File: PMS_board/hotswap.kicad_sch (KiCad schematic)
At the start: 22 parts, among them Q5 Q_NMOS_GDS, Q6 Q_NMOS_GDS, Q7 Q_NMOS_GDS, Q8 Q_NMOS_GDS, U12 LM74800QDRRRQ1, U9 LM74800QDRRRQ1

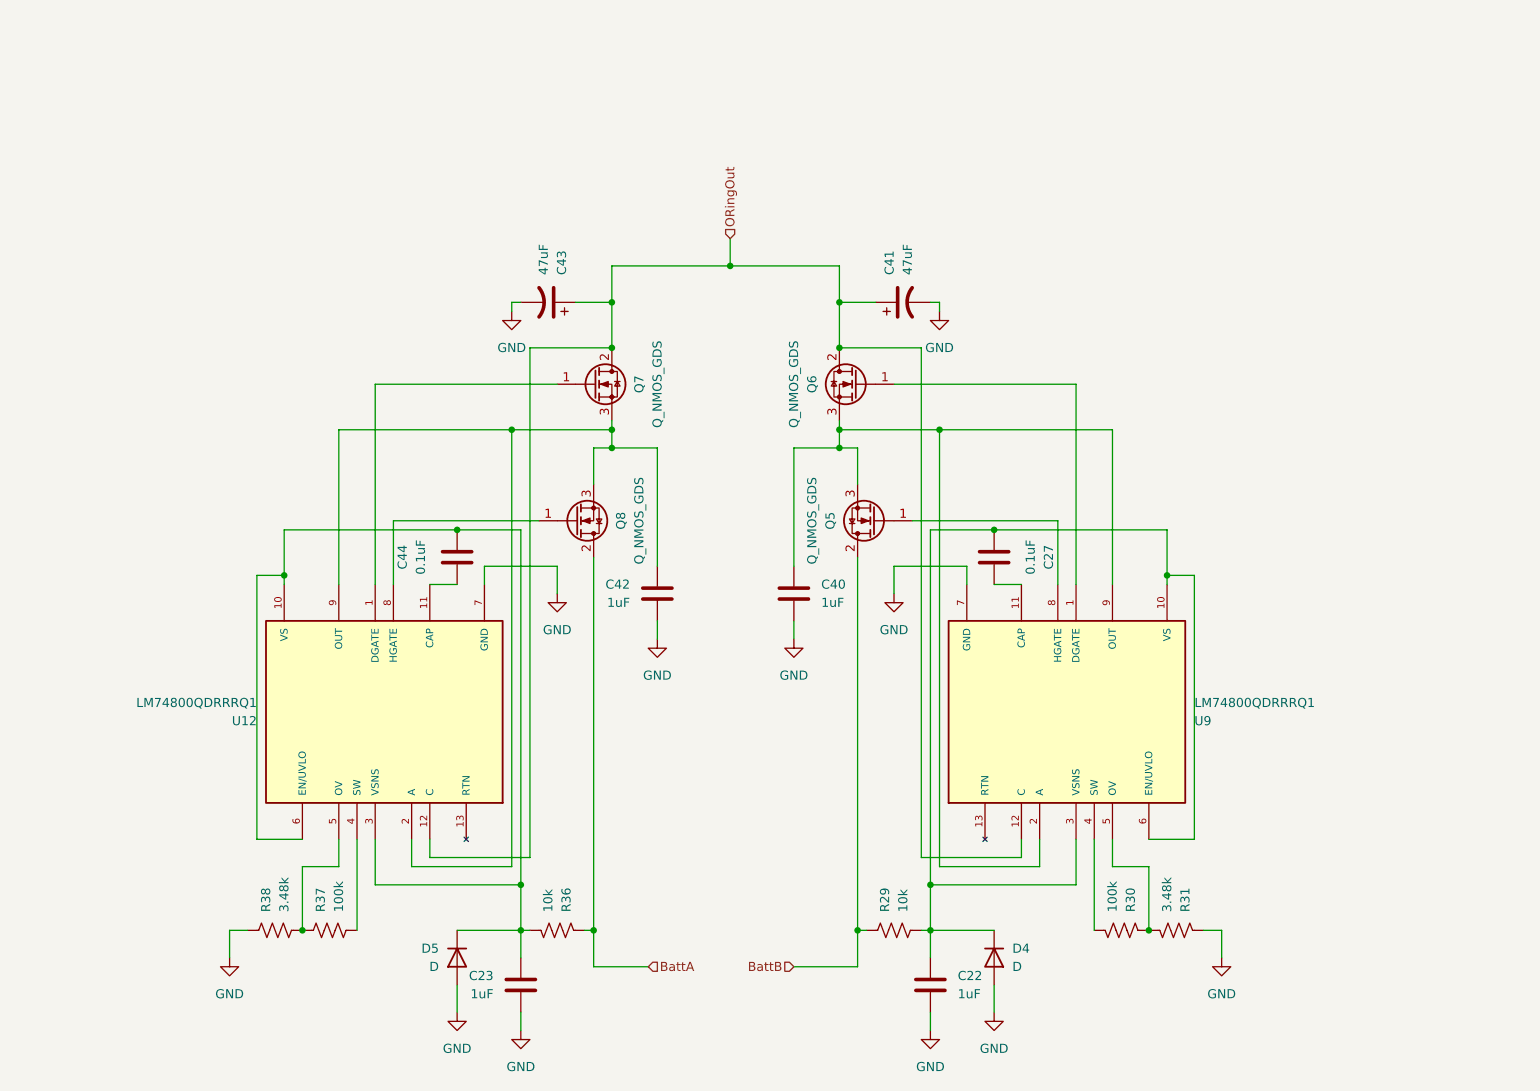
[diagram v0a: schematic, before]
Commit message: add power smoothing
I added the majority (i hope) of the necessary components for power smoothing and conversion. I also added notes to remind me and to inform others in my absence as to what still needs to be done to my knowledge.
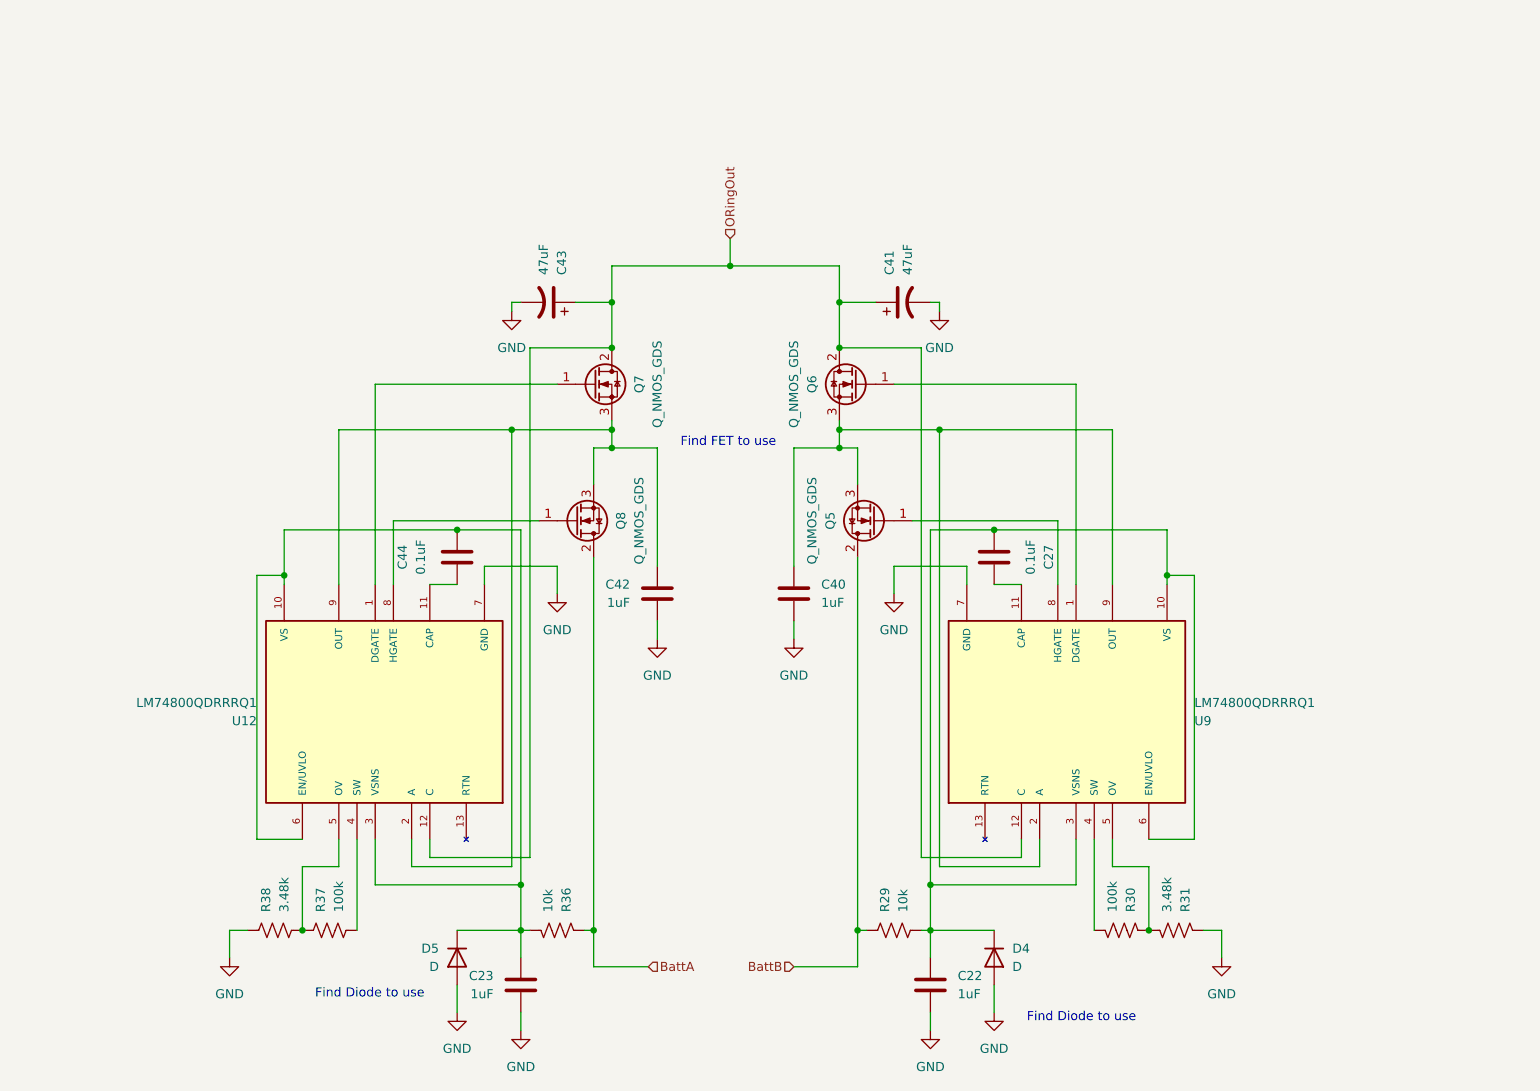
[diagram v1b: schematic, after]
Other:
- note added: "Find Diode to use"
- note added: "Find FET to use"
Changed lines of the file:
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@@
 	(generator_version "10.0")
 	(paper "A4")
+	(text "Find Diode to use\n"
+		(exclude_from_sim no)
+		(at 162.052 153.162 0)
+		(effects
+			(font
+				(size 1.27 1.27)
+			)
+		)
+	)
+	(text "Find FET to use\n"
+		(exclude_from_sim no)
+		(at 112.776 72.898 0)
+		(effects
+			(font
+				(size 1.27 1.27)
+			)
+		)
+	)
+	(text "Find Diode to use\n"
+		(exclude_from_sim no)
+		(at 62.738 149.86 0)
+		(effects
+			(font
+				(size 1.27 1.27)
+			)
+		)
+	)
 	(junction
 		(at 128.27 71.12)

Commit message: add converter and friends
I added the converter symbols and updated the schematic. I chose the proper FETs and Diodes for ORing circuit.
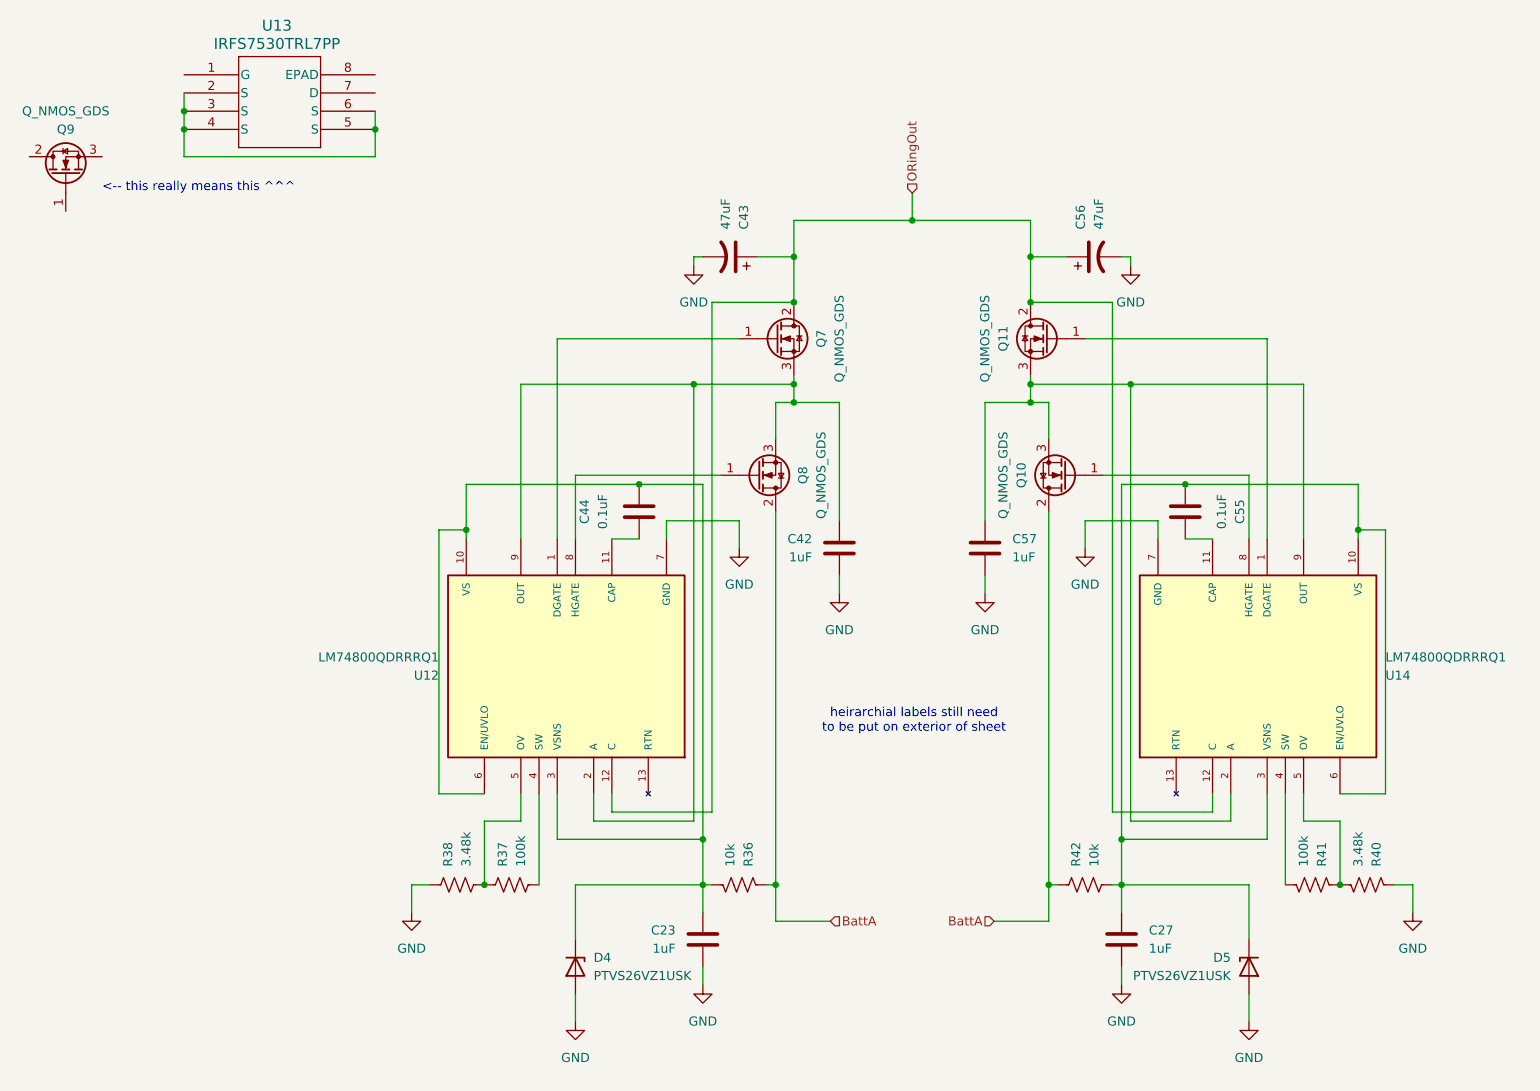
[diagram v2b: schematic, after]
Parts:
- removed C22, C40: 1uF, symbol Device:C
- removed C41: 47uF, symbol Device:C_Polarized_US
- removed D4, D5: D, symbol Device:D
- removed Q5, Q6: Q_NMOS_GDS, symbol Transistor_FET:Q_NMOS_GDS
- removed R29: 10k, symbol Device:R_US
- removed R30: 100k, symbol Device:R_US
- removed R31: 3.48k, symbol Device:R_US
- removed U9: LM74800QDRRRQ1, LM74800QDRRRQ1:IC_LM74800QDRRRQ1, symbol LM74800QDRRRQ1:LM74800QDRRRQ1
- added C55: 0.1uF, symbol Device:C
- added C56: 47uF, symbol Device:C_Polarized_US
- added C57: 1uF, symbol Device:C
- added D4, D5: PTVS26VZ1USK, Diode_SMD:Nexperia_DSN1608-2_1.6x0.8mm, symbol Diode:PTVS26VZ1USK
- added Q10, Q11, Q9: Q_NMOS_GDS, symbol Transistor_FET:Q_NMOS_GDS
- added R40: 3.48k, symbol Device:R_US
- added R41: 100k, symbol Device:R_US
- added R42: 10k, symbol Device:R_US
- added U13: IRFS7530TRL7PP, PG-TO263-7_INF, symbol IRFS7530TRL7PP:IRFS7530TRL7PP
- added U14: LM74800QDRRRQ1, LM74800QDRRRQ1:IC_LM74800QDRRRQ1, symbol LM74800QDRRRQ1:LM74800QDRRRQ1
- C27: value 0.1uF -> 1uF
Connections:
- net BattA: now also Q10.2 (D), R42.1
- net GND: now also C27.2, C56.2, C57.2, D4.2 (A), D5.2 (A), R40.1, U14.7 (GND)
- net ORingOut: now also C56.1, Q11.2 (D), U14.12 (C)
- net at C27.1: now also C55.2, D5.1 (K), R42.2, U14.10 (VS), U14.3 (VSNS), U14.6 (EN/UVLO)
- net at C23.1, C44.2, R36.2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: now also D4.1 (K)
- new net: R40.2, R41.1, U14.5 (OV)
- new net: R41.2, U14.4 (SW)
- new net: Q10.1 (G), U14.8 (HGATE)
- new net: C57.1, Q10.3 (S), Q11.3 (S), U14.2 (A), U14.9 (OUT)
- new net: Q11.1 (G), U14.1 (DGATE)
- new net: C55.1, U14.11 (CAP)
- new net: U13.2 (S), U13.3 (S), U13.4 (S), U13.5 (S), U13.6 (S)
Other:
- note added: "<-- this really means this ^^^"
- note added: "heirarchial labels still need to be put on exterior of sheet"
- note removed: "Find Diode to use"
- note removed: "Find FET to use"
- moved on the sheet: C23, C42, C43, C44, Q7, Q8, R36, R37, R38, U12

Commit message: Add Bucks & Fix Issues
- Added 3V3 and 5V buck convertors
- Removed Pi filter
- adjusted capacitor values for Bulk Capacitors
- Added inrush protection to ORing circuit
- renamed various hierarchical pins for clarity
- renamed power rail pins due to naming conflicts
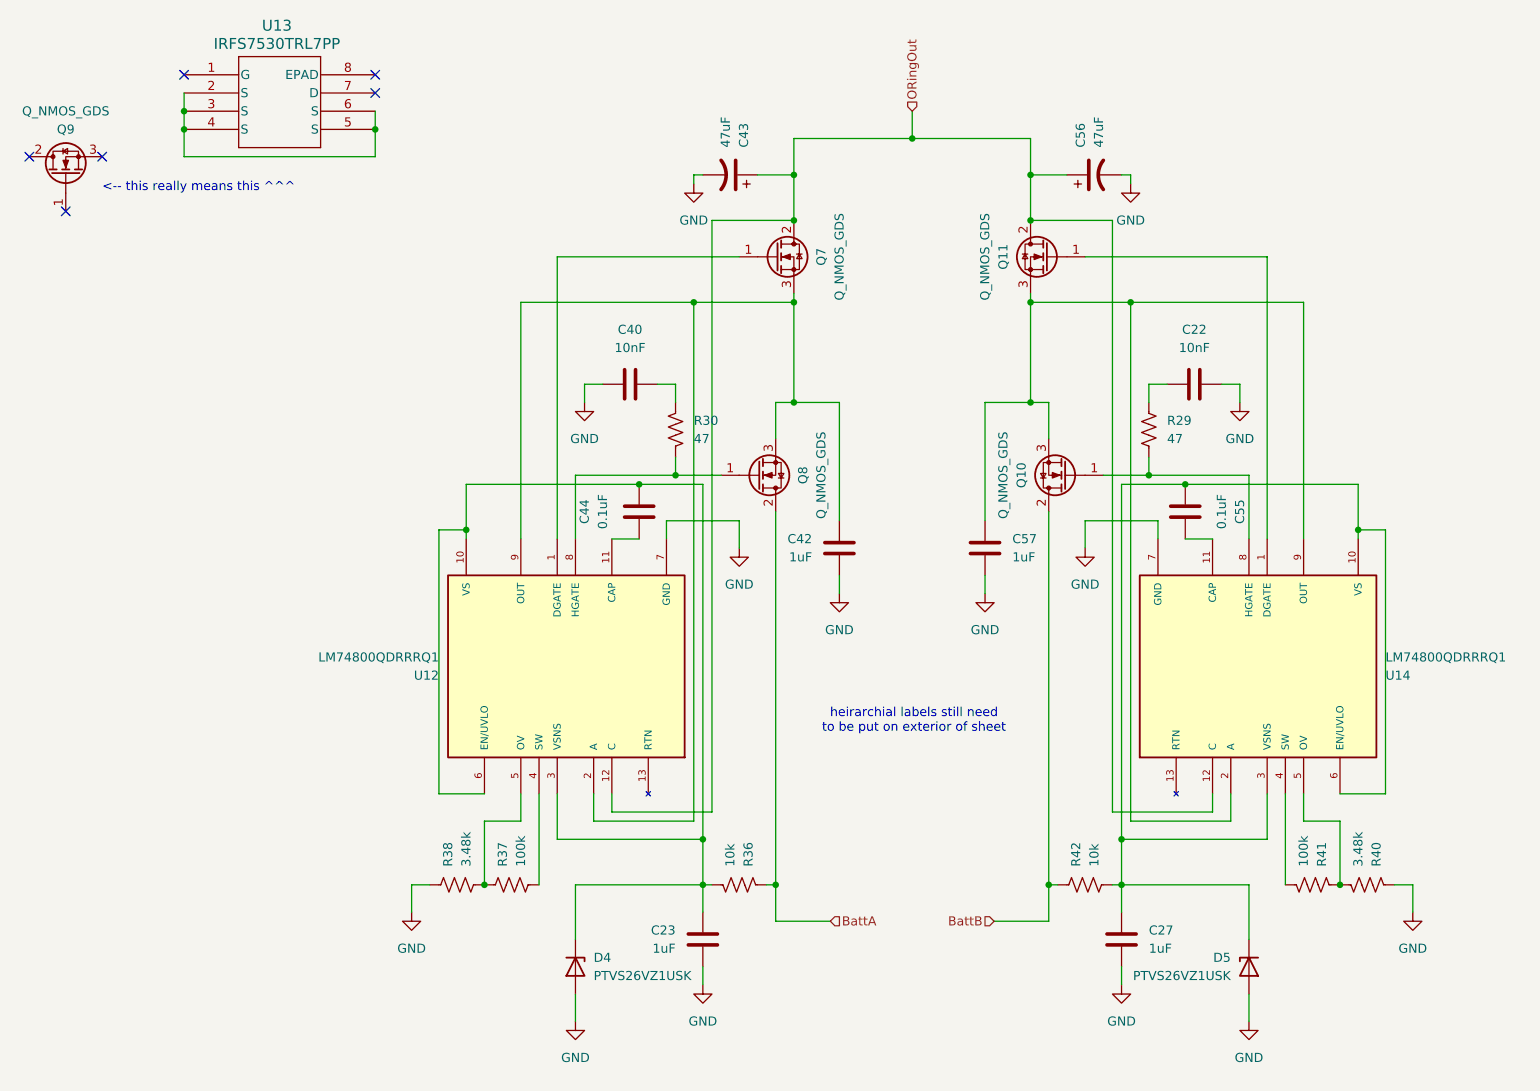
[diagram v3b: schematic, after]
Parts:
- added C22, C40: 10nF, symbol Device:C
- added R29, R30: 47, symbol Device:R_US
- Q9, U13: now left out of the parts list
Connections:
- net BattA: no longer Q10.2 (D), R42.1
- net GND: now also C22.2, C40.2
- net at Q10.1 (G), U14.8 (HGATE): now also R29.2
- net at Q8.1 (G), U12.8 (HGATE): now also R30.2
- new net: C22.1, R29.1
- new net: C40.1, R30.1
- new net BattB: Q10.2 (D), R42.1
- no-connect marks 0 -> 6
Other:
- moved on the sheet: C43, C56, Q11, Q7

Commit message: Refine Current Sensing
- Removed redundant current sensors
- Fixed hierarchical labelling for sensors
- added labeling for a few circuits
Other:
- note removed: "heirarchial labels still need to be put on exterior of sheet"
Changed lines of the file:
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@@
-		)
-	)
-	(text "heirarchial labels still need\nto be put on exterior of sheet"
-		(exclude_from_sim no)
-		(at 138.684 111.76 0)
-		(effects
-			(font
-				(size 1.27 1.27)
-			)
 		)
 	)

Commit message: Finish Schematic
There's definitely stuff I missed, but I'm tired so we can review later. For my members to keep track of things, these are the changes/last minute additions I ran out of time to teach:
- brake chopper circuitry & reverse voltage protection for aux & motor rails
- microcontroller pinnouts
- net connections between sheets
- voltage resistors & system voltage measurements
- cell sense connectors & switch
- ADC routing
Please Please PLEASE ask questions about these additions. I don't want you guys to feel like you don't own this schematic, and I'm sorry I had to take away some of these designs to finish early. I definitely left too much on your plate to get everything perfect, which is my bad. I will happily walk through each and every circuit and help explain each part so you can better know your project when we get to reviewing and debugging later down the line.
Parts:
- removed C40: 10nF, symbol Device:C
- removed R36: 10k, symbol Device:R_US
- removed U13: IRFS7530TRL7PP, PG-TO263-7_INF, symbol IRFS7530TRL7PP:IRFS7530TRL7PP
- added C60: 10nF, symbol Device:C
- added R91: 10k, symbol Device:R_US
- added U18: IRFS7530TRL7PP, PG-TO263-7_INF, symbol IRFS7530TRL7PP:IRFS7530TRL7PP
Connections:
- net BattA: now also R91.1
- net GND: now also C60.2
- net at C23.1, C44.2, D4.1 (K)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: now also R91.2
- net at R30.1: now also C60.1
- new net: U18.2 (S), U18.3 (S), U18.4 (S), U18.5 (S), U18.6 (S)

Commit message: Add Footprints & such
whoops forgot to push yesterday teehee
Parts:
- C22, C23, C27, C42, C43, C44, C55, C56, C57, C60: footprint (none) -> Capacitor_SMD:C_0603_1608Metric
- Q10, Q11, Q7, Q8: footprint (none) -> IRFS7530TRL7PP:PG-TO263-7_INF-M
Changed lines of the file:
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@@
 			)
 		)
-		(property "Footprint" ""
+		(property "Footprint" "Capacitor_SMD:C_0603_1608Metric"
 			(at 168.6052 146.05 0)
 			(hide yes)
@@
 			)
 		)
-		(property "Footprint" ""
+		(property "Footprint" "Capacitor_SMD:C_0603_1608Metric"
 			(at 181.61 63.8048 0)
 			(hide yes)
@@
 			)
 		)
-		(property "Footprint" ""
+		(property "Footprint" "IRFS7530TRL7PP:PG-TO263-7_INF-M"
 			(at 154.94 80.01 0)
 			(hide yes)
@@
 			)
 		)
-		(property "Footprint" ""
+		(property "Footprint" "Capacitor_SMD:C_0603_1608Metric"
 			(at 108.2548 146.05 0)
 			(hide yes)
@@
 			)
 		)
-		(property "Footprint" ""
+		(property "Footprint" "Capacitor_SMD:C_0603_1608Metric"
 			(at 99.3648 78.74 0)
 			(hide yes)
@@
 			)
 		)
-		(property "Footprint" ""
+		(property "Footprint" "Capacitor_SMD:C_0603_1608Metric"
 			(at 95.25 63.8048 0)
 			(hide yes)
@@
 			)
 		)
-		(property "Footprint" ""
+		(property "Footprint" "Capacitor_SMD:C_0603_1608Metric"
 			(at 129.2352 91.44 0)
 			(hide yes)
@@
 			)
 		)
-		(property "Footprint" ""
+		(property "Footprint" "IRFS7530TRL7PP:PG-TO263-7_INF-M"
 			(at 152.4 44.45 0)
 			(hide yes)
@@
 			)
 		)
-		(property "Footprint" ""
+		(property "Footprint" "IRFS7530TRL7PP:PG-TO263-7_INF-M"
 			(at 124.46 44.45 0)
 			(hide yes)
@@
 			)
 		)
-		(property "Footprint" ""
+		(property "Footprint" "Capacitor_SMD:C_0603_1608Metric"
 			(at 163.83 35.56 0)
 			(hide yes)
@@
 			)
 		)
-		(property "Footprint" ""
+		(property "Footprint" "Capacitor_SMD:C_0603_1608Metric"
 			(at 177.4952 78.74 0)
 			(hide yes)
@@
 			)
 		)
-		(property "Footprint" ""
+		(property "Footprint" "Capacitor_SMD:C_0603_1608Metric"
 			(at 113.03 35.56 0)
 			(hide yes)
@@
 			)
 		)
-		(property "Footprint" ""
+		(property "Footprint" "IRFS7530TRL7PP:PG-TO263-7_INF-M"
 			(at 121.92 80.01 0)
 			(hide yes)
@@
 			)
 		)
-		(property "Footprint" ""
+		(property "Footprint" "Capacitor_SMD:C_0603_1608Metric"
 			(at 147.6248 91.44 0)
 			(hide yes)
